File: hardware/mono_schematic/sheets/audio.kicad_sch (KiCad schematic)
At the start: 11 parts

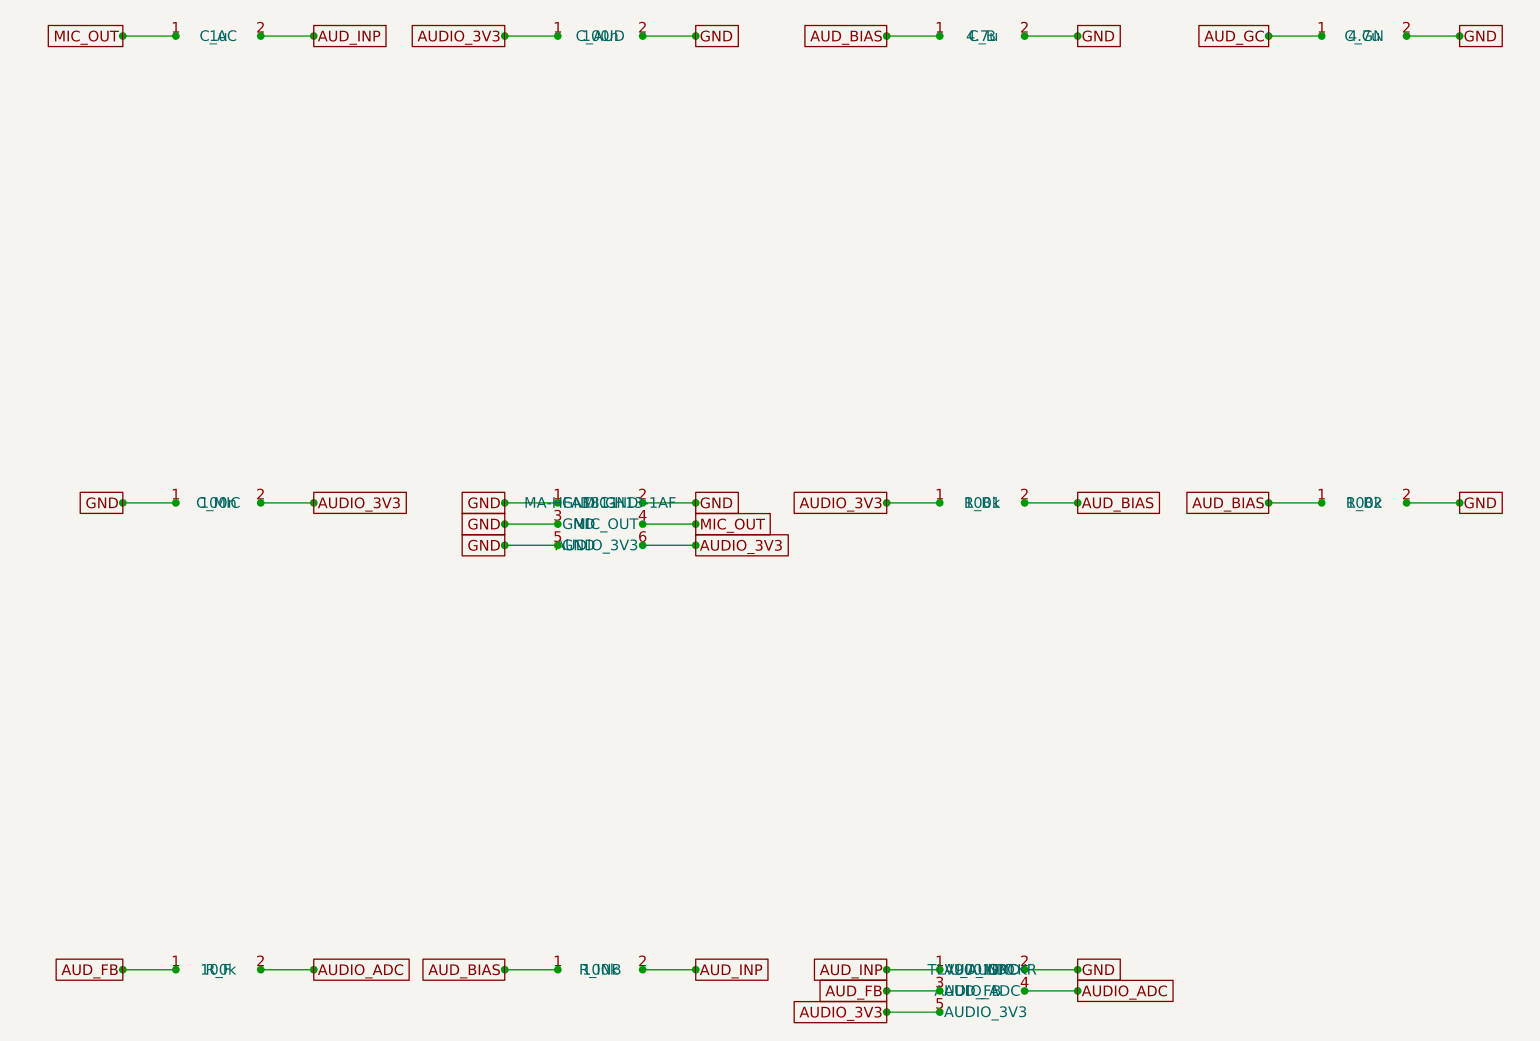
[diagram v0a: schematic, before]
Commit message: mono_electronics v11b: TLV75733P 1A AON LDO, 22uF ESP32 bulk, LED_EN RC glitch filter, J_USB value, refs end in digit; schematic regenerated (ERC 0, 0 diffs)
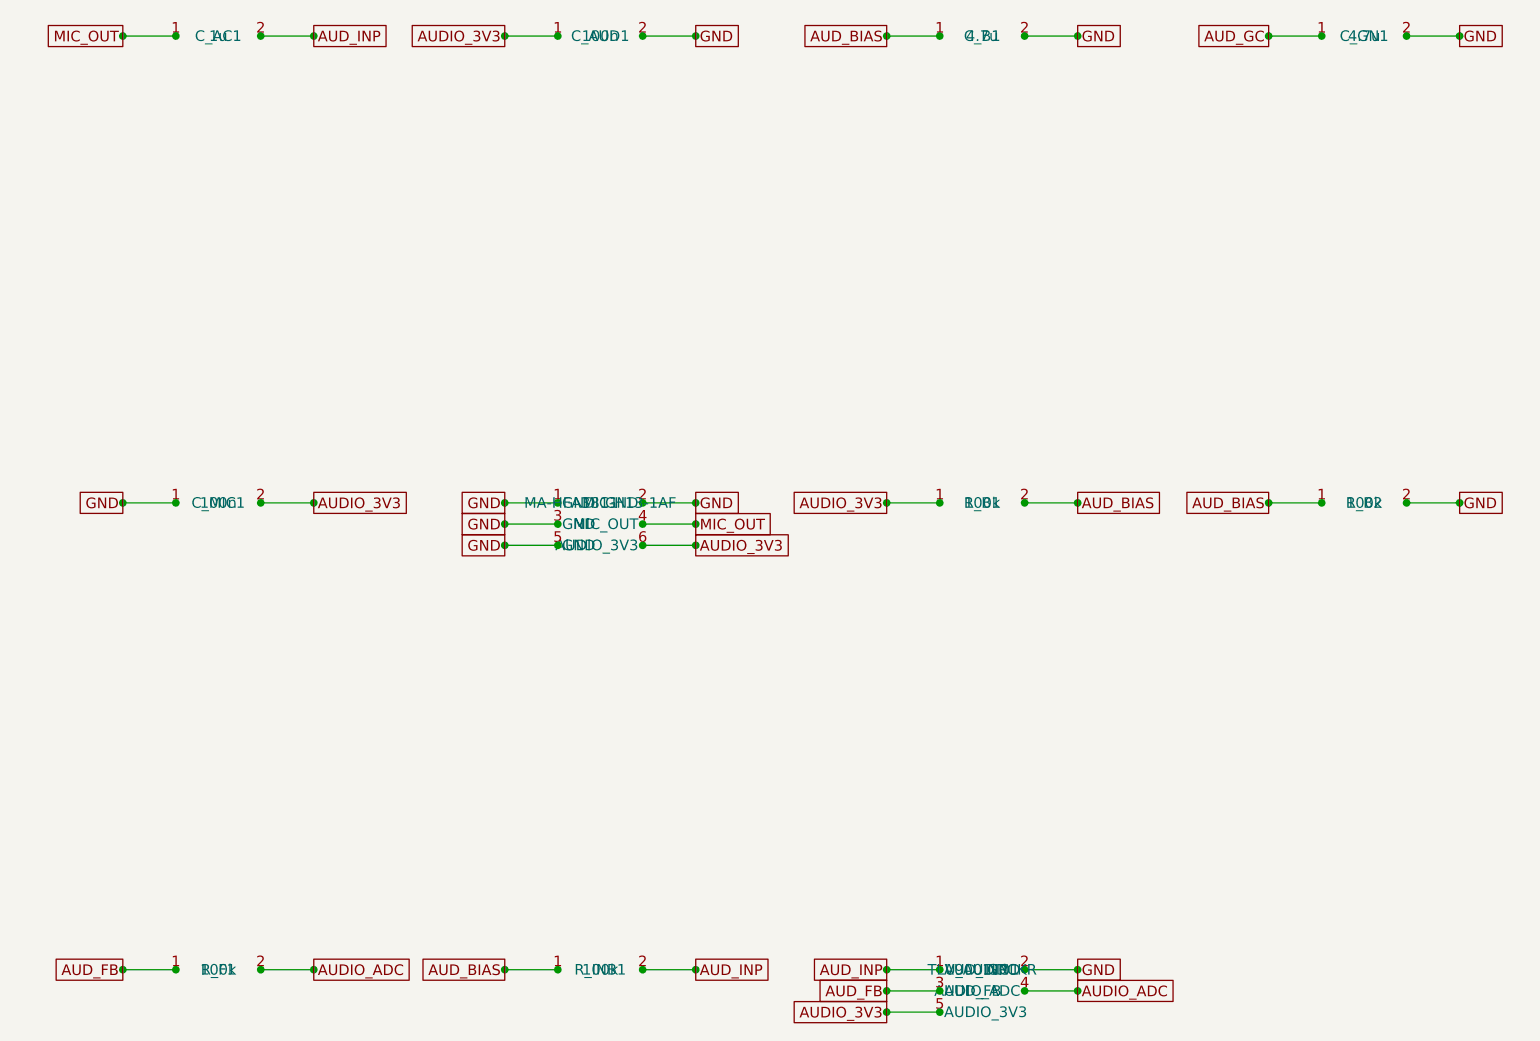
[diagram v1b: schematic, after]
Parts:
- removed C_AC: 1u, mono_electronics:C_0402_1005Metric, symbol mono_parts:1u_C_0402_1005Metric_2
- removed C_AUD, C_MIC: 100n, mono_electronics:C_0402_1005Metric, symbol mono_parts:100n_C_0402_1005Metric_2
- removed C_B, C_GN: 4.7u, mono_electronics:C_0402_1005Metric, symbol mono_parts:4.7u_C_0402_1005Metric_2
- removed R_F, R_INB: 100k, mono_electronics:R_0402_1005Metric, symbol mono_parts:100k_R_0402_1005Metric_2
- removed U_AUDIO: TLV9001IDCKR, mono_electronics:SOT-353_SC-70-5, symbol mono_parts:TLV9001IDCKR_SOT-353_SC-70-5_5
- added C_AC1: 1u, mono_electronics:C_0402_1005Metric, symbol mono_parts:1u_C_0402_1005Metric_2
- added C_AUD1, C_MIC1: 100n, mono_electronics:C_0402_1005Metric, symbol mono_parts:100n_C_0402_1005Metric_2
- added C_B1, C_GN1: 4.7u, mono_electronics:C_0402_1005Metric, symbol mono_parts:4.7u_C_0402_1005Metric_2
- added R_F1, R_INB1: 100k, mono_electronics:R_0402_1005Metric, symbol mono_parts:100k_R_0402_1005Metric_2
- added U_AUDIO1: TLV9001IDCKR, mono_electronics:SOT-353_SC-70-5, symbol mono_parts:TLV9001IDCKR_SOT-353_SC-70-5_5
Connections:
- net AUDIO_3V3: now also C_AUD1.1, C_MIC1.2, U_AUDIO1.5 (AUDIO_3V3)
- net AUDIO_ADC: now also R_F1.2, U_AUDIO1.4 (AUDIO_ADC)
- net AUD_BIAS: now also C_B1.1, R_INB1.1
- net AUD_FB: now also R_F1.1, U_AUDIO1.3 (AUD_FB)
- net AUD_GC: now also C_GN1.1
- net AUD_INP: now also C_AC1.2, R_INB1.2, U_AUDIO1.1 (AUD_INP)
- net GND: now also C_AUD1.2, C_B1.2, C_GN1.2, C_MIC1.1, U_AUDIO1.2 (GND)
- net MIC_OUT: now also C_AC1.1
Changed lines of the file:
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@@
     (property
       "Reference"
-      "C_AC"
+      "C_AC1"
       (at 35.56 35.56 0)
       (effects
@@
     (instances
       (project "mono_electronics"
-        (path "/ee49b9cd-faa6-4f95-ac43-f5e18ee90ff0"
-          (reference "C_AC")
+        (path "/03c9e6d7-0f21-4731-9314-2880fc5ad417"
+          (reference "C_AC1")
           (unit 1)
         )
@@
     (property
       "Reference"
-      "C_AUD"
+      "C_AUD1"
       (at 81.28 35.56 0)
       (effects
@@
     (instances
       (project "mono_electronics"
-        (path "/ee49b9cd-faa6-4f95-ac43-f5e18ee90ff0"
-          (reference "C_AUD")
+        (path "/03c9e6d7-0f21-4731-9314-2880fc5ad417"
+          (reference "C_AUD1")
           (unit 1)
         )
@@
     (property
       "Reference"
-      "C_B"
+      "C_B1"
       (at 127 35.56 0)
       (effects
@@
     (instances
       (project "mono_electronics"
-        (path "/ee49b9cd-faa6-4f95-ac43-f5e18ee90ff0"
-          (reference "C_B")
+        (path "/03c9e6d7-0f21-4731-9314-2880fc5ad417"
+          (reference "C_B1")
           (unit 1)
         )
@@
     (property
       "Reference"
-      "C_GN"
+      "C_GN1"
       (at 172.72 35.56 0)
       (effects
@@
     (instances
       (project "mono_electronics"
-        (path "/ee49b9cd-faa6-4f95-ac43-f5e18ee90ff0"
-          (reference "C_GN")
+        (path "/03c9e6d7-0f21-4731-9314-2880fc5ad417"
+          (reference "C_GN1")
           (unit 1)
         )
@@
     (property
       "Reference"
-      "C_MIC"
+      "C_MIC1"
       (at 35.56 91.44 0)
       (effects
@@
     (instances
       (project "mono_electronics"
-        (path "/ee49b9cd-faa6-4f95-ac43-f5e18ee90ff0"
-          (reference "C_MIC")
+        (path "/03c9e6d7-0f21-4731-9314-2880fc5ad417"
+          (reference "C_MIC1")
           (unit 1)
         )
@@
     (instances
       (project "mono_electronics"
-        (path "/ee49b9cd-faa6-4f95-ac43-f5e18ee90ff0"
+        (path "/03c9e6d7-0f21-4731-9314-2880fc5ad417"
           (reference "MIC1")
           (unit 1)
@@
     (instances
       (project "mono_electronics"
-        (path "/ee49b9cd-faa6-4f95-ac43-f5e18ee90ff0"
+        (path "/03c9e6d7-0f21-4731-9314-2880fc5ad417"
           (reference "R_B1")
           (unit 1)
@@
     (instances
       (project "mono_electronics"
-        (path "/ee49b9cd-faa6-4f95-ac43-f5e18ee90ff0"
+        (path "/03c9e6d7-0f21-4731-9314-2880fc5ad417"
           (reference "R_B2")
           (unit 1)
@@
     (property
       "Reference"
-      "R_F"
+      "R_F1"
       (at 35.56 147.32 0)
       (effects
@@
     (instances
       (project "mono_electronics"
-        (path "/ee49b9cd-faa6-4f95-ac43-f5e18ee90ff0"
-          (reference "R_F")
+        (path "/03c9e6d7-0f21-4731-9314-2880fc5ad417"
+          (reference "R_F1")
           (unit 1)
         )
@@
     (property
       "Reference"
-      "R_INB"
+      "R_INB1"
       (at 81.28 147.32 0)
       (effects
@@
     (instances
       (project "mono_electronics"
-        (path "/ee49b9cd-faa6-4f95-ac43-f5e18ee90ff0"
-          (reference "R_INB")
+        (path "/03c9e6d7-0f21-4731-9314-2880fc5ad417"
+          (reference "R_INB1")
           (unit 1)
         )
@@
     (property
       "Reference"
-      "U_AUDIO"
+      "U_AUDIO1"
       (at 127 147.32 0)
       (effects
@@
     (instances
       (project "mono_electronics"
-        (path "/ee49b9cd-faa6-4f95-ac43-f5e18ee90ff0"
-          (reference "U_AUDIO")
+        (path "/03c9e6d7-0f21-4731-9314-2880fc5ad417"
+          (reference "U_AUDIO1")
           (unit 1)
         )
@@
   )
   (sheet_instances
-    (path "/ee49b9cd-faa6-4f95-ac43-f5e18ee90ff0"
+    (path "/03c9e6d7-0f21-4731-9314-2880fc5ad417"
       (page "1")
     )
